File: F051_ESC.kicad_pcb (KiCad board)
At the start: 4 copper layers, 41 x 20 mm, 64 parts, among them J1 Conn_01x02, J2 Conn_01x04, J3 Conn_01x04, J4 Conn_01x03, J5 Conn_01x01, J6 Conn_01x02, Q1 TPHR8504PL, Q2 TPHR8504PL, Q3 TPHR8504PL, Q4 TPHR8504PL, Q5 TPHR8504PL, Q6 TPHR8504PL, U1 FD6288Q, U2 STM32F051K6Ux, U3 L78L12_SOT89, U4 LP2985-3.3, U5 INA139, U7 OPA340NA

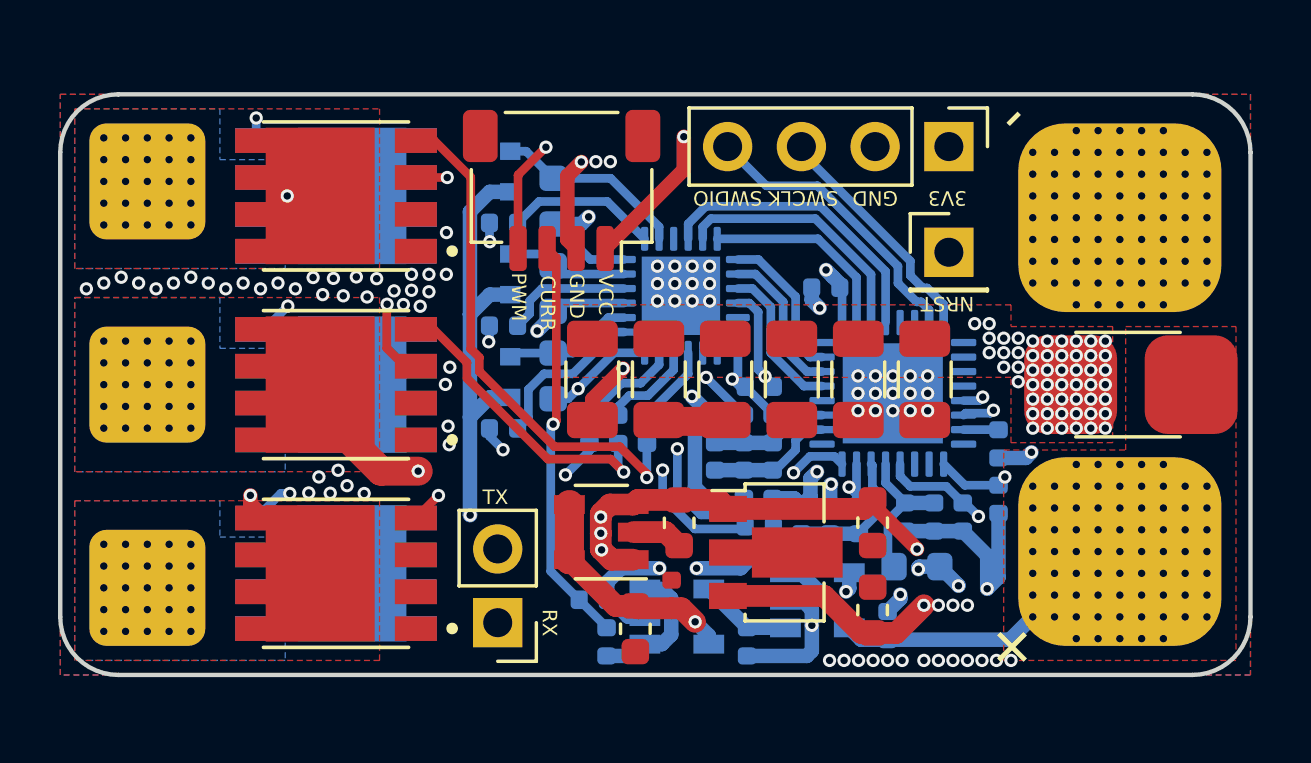
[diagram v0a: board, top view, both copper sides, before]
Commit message: Rerouting of a lot of layers
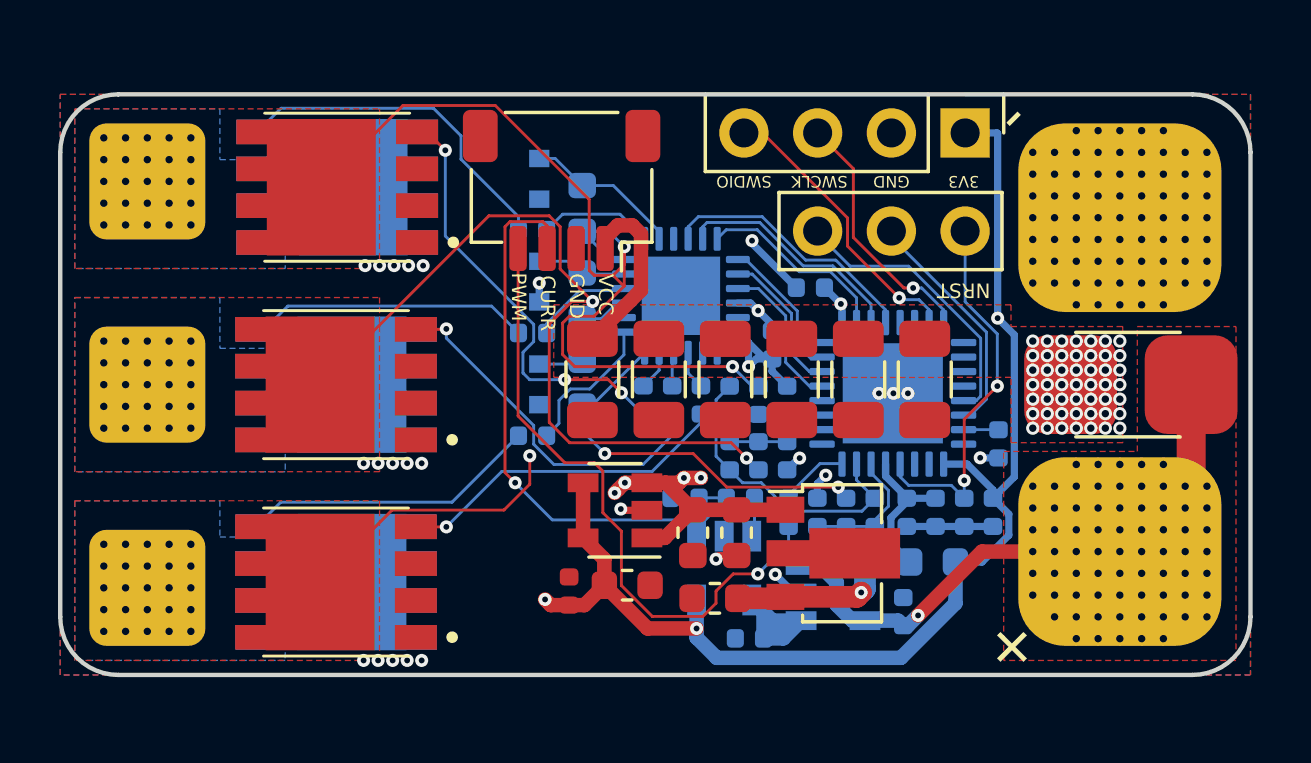
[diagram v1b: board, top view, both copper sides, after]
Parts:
- removed J5: Conn_01x01, Connector_PinHeader_2.54mm:PinHeader_1x01_P2.54mm_Vertical
- J6: value Conn_01x02 -> Conn_01x03; footprint Connector_PinHeader_2.54mm:PinHeader_1x02_P2.54mm_Vertical -> Connector_PinHeader_2.54mm:PinHeader_1x03_P2.54mm_Vertical
- R1: value 5m -> 1m
- R14, R17, R19: value 3.93k -> 10k
- moved J6 21.0 mm to (250.2, 74.7), turned to 270 degrees
- moved Q1 13.3 mm to (228.5, 73.2)
- moved Q2 13.3 mm to (228.5, 73.2)
- moved Q5 13.3 mm to (228.5, 86.8)
- moved Q6 13.3 mm to (228.5, 86.8)
- moved R3 6.77 mm to (242.4, 83.9), turned to 0 degrees
- moved C4 5.45 mm to (241.6, 87.4), turned to 180 degrees
- moved C8 4.72 mm to (240.5, 83.9), turned to 0 degrees
- moved C5 4.70 mm to (242.3, 85.1)
- moved C23 3.53 mm to (236.5, 87.1)
- moved U7 2.33 mm to (241.9, 86.3), turned to 270 degrees
- moved R10 2.12 mm to (240.1, 80.5)
- moved R8 2.12 mm to (239.1, 80.5)
- moved R12 2.12 mm to (241.1, 80.5)
- moved U3 1.98 mm to (245.6, 85.8)
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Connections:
- J4 pad 1: /MCU/PhaseA -> /MCU/PhaseC
- J4 pad 3: /MCU/PhaseC -> /MCU/PhaseA
- J6 pad 1: /MCU/USART1_RX -> /MCU/NRST
- J6 pad 2: /MCU/USART1_TX -> /MCU/USART1_RX
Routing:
- net +12V: track 58.8 -> 20.0 mm
- net GND: track 46.8 -> 15.2 mm, vias 145 -> 83
- net /MCU/USART1_RX: track 21.4 -> 7.95 mm, vias 1 -> 0
- net /MCU/USART1_TX: track 20.1 -> 9.71 mm, vias 1 -> 0
- net /MCU/PhaseC: track 36.4 -> 26.1 mm
- net VCC: track 9.93 -> 20.1 mm
- net Net-(Q5-Pad4): track 19.8 -> 10.3 mm, vias 2 -> 0
- net Net-(Q2-Pad4): track 7.19 -> 15.1 mm, vias 2 -> 3
- net Net-(R24-Pad1): track 10.1 -> 2.41 mm, vias 2 -> 0
- net Net-(Q6-Pad4): track 18.2 -> 12.1 mm
- net +3V3: track 44.2 -> 50.2 mm, vias 5 -> 4
- net /Curent Sense/CURR: track 14.1 -> 19.4 mm
- net Net-(Q1-Pad4): track 15.7 -> 11.8 mm, vias 2 -> 0
- net /MCU/SenseCOM: track 14.2 -> 10.7 mm, vias 2 -> 0
- net Net-(R2-Pad1): track 3.20 -> 5.74 mm
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- added copper zone on In2.Cu, net +12V
- added copper zone on B.Cu, net GND
- removed copper zone on B.Cu, net VCC_Shunt
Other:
- net class Default: clearance 0.127 -> 0.1; trace_width 0.127 -> 0.1; via_dia 0.4572 -> 0.45; via_drill 0.254 -> 0.2
- net class Min added: clearance 0.1, trace_width 0.1, via_dia 0.45, via_drill 0.2
- rule trace_clearance: 0.127 -> 0.1
- rule trace_min: 0.127 -> 0.1
- rule via_min_drill: 0.254 -> 0.2
- rule via_min_size: 0.4572 -> 0.45
- board text removed: "RX"
- board text removed: "TX"

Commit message: Added vias and a little bit of rearranging
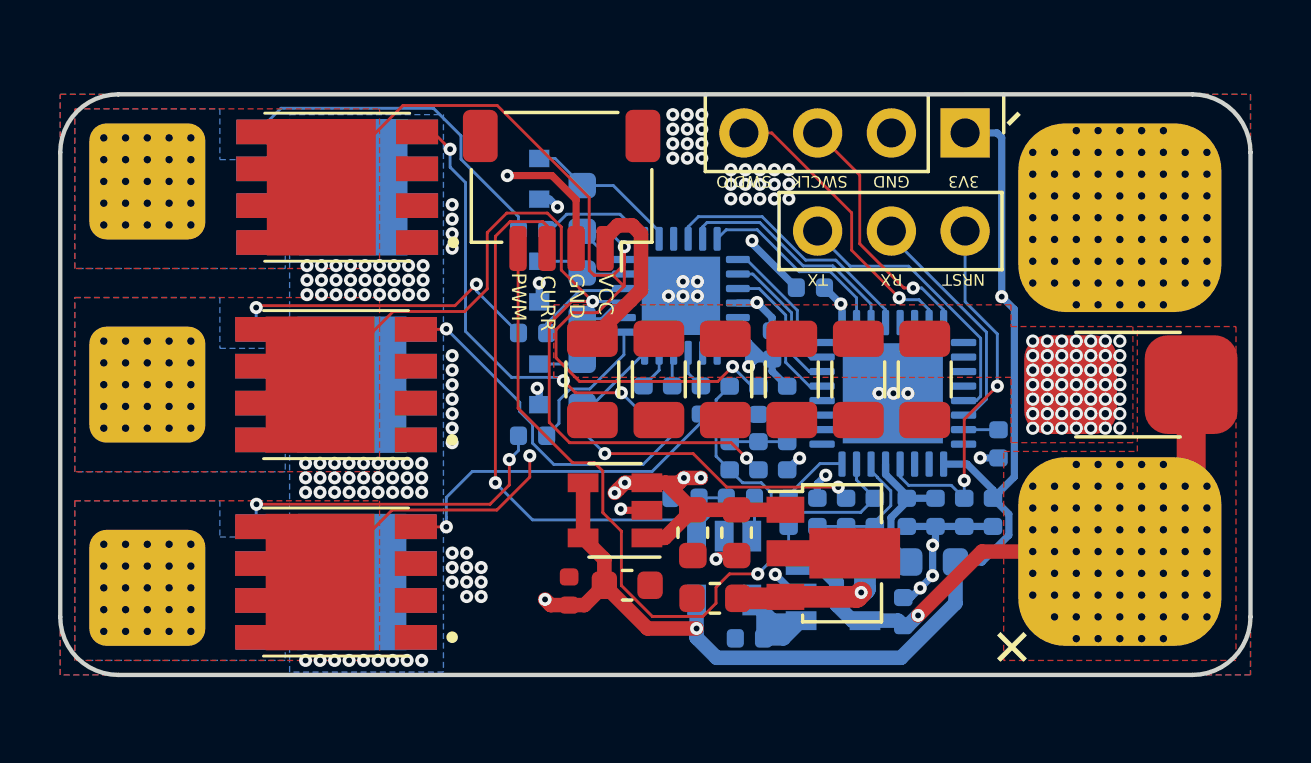
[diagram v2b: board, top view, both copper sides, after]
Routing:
- net GND: track 15.2 -> 23.1 mm, vias 83 -> 140
- net /MCU/PhaseB: track 29.4 -> 31.7 mm
- net +12V: track 20.0 -> 21.8 mm, vias 6 -> 8
- net /MCU/PhaseA: track 32.6 -> 33.9 mm
- net Net-(Q5-Pad4): track 10.3 -> 11.6 mm, vias 0 -> 2
- net Net-(Q3-Pad4): track 9.75 -> 10.9 mm, vias 0 -> 2
- net /Curent Sense/CURR: track 19.4 -> 20.1 mm
- net Net-(Q6-Pad4): track 12.1 -> 12.7 mm
- net VCC_Shunt: vias 65 -> 113
- added copper zone on B.Cu, net VCC_Shunt
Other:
- board text added: "RX"
- board text added: "TX"
